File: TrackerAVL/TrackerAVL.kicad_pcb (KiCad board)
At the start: 2 copper layers, 174 parts, among them J801 Conn_02x07_Odd_Even, J802 Conn_01x15, J803 Conn_01x04, P201 uC_debug, Q201 DTC043ZEBTL, Q202 DTC043ZEBTL, Q203 DTC043ZEBTL, Q701 2N7002P, Q702 2N7002P, Q703 2N7002P, Q704 DTC043ZEBTL, U201 MAX3221, U202 LPC4337JBD144, U203 STS8C5H30L, U301 MPU-6050, U401 NAU8814, U501 STS8C5H30L, U502 LD1085D2T33R, U503 NCP114ASN180T1G, U601 MPCIE-Socket, U701 74LVC244APW, U801 74HC4053, X201 12MHz, X202 32.768K

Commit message: Cambios en pcb
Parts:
- moved D704 218.5 mm to (314.0, 128.9)
- moved D709 218.5 mm to (318.7, 126.6)
- moved Q701 218.5 mm to (309.2, 127.4)
- moved U301 218.5 mm to (301.2, 145.8)
- moved C302 218.5 mm to (304.2, 149.4)
- moved C304 218.5 mm to (300.4, 149.4)
- moved C501 218.5 mm to (252.3, 143.5)
- moved C502 218.5 mm to (262.6, 130.9)
- moved C503 218.5 mm to (252.3, 141.6)
- moved C506 218.5 mm to (262.6, 132.8)
- moved C701 218.5 mm to (321.9, 128.5)
- moved C702 218.5 mm to (309.9, 138.3)
- moved C703 218.5 mm to (314.7, 132.8)
- moved C704 218.5 mm to (309.9, 136.4)
- moved C705 218.5 mm to (317.4, 136.7)
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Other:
- board outline added: 100 x 70 mm
- net class Default: clearance 0.2 -> 0.25; via_dia 0.8 -> 1; via_drill 0.4 -> 0.5
- rule trace_clearance: 0.2 -> 0.25
- rule trace_min: 0.2 -> 0.25
- rule via_min_drill: 0.3 -> 0.4
- rule via_min_size: 0.4 -> 0.8
- board text added: "Equipo AVL vRaptor v1.0 Referencia: Mayer (Tecnología 8 mils) Grillas: 1mm, 0,5mm, 0,25mm Vía: 1mm - Agujero: 0,5mm Márgen: 0,25mm Pista más delgada: 0,25mm Dist. a borde: 0,3mm STACK-UP FR4 1,6mm Dual layer Componentes en capa superior Máscara anti-soldante: Azul Sin requerimientos especiales Terminación: HASL c/Pb Espesor de Cu: 1oz"

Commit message: Cambios en pcb
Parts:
- moved C404 239.4 mm to (112.3, 47.6)
- moved C405 239.4 mm to (108.6, 49.5)
- moved C410 239.4 mm to (116.1, 49.5)
- moved C418 239.4 mm to (112.3, 49.5)
- moved C419 239.4 mm to (116.1, 47.6)
- moved JP401 239.4 mm to (121.8, 55.7)
- moved R402 239.4 mm to (108.6, 47.6)
- moved R403 239.4 mm to (123.6, 47.6)
- moved R404 239.4 mm to (123.6, 49.5)
- moved R409 239.4 mm to (119.8, 49.5)
- moved R412 239.4 mm to (119.8, 47.6)
- moved U401 239.4 mm to (104.0, 49.3)
- moved C401 239.4 mm to (110.7, 51.5)
- moved C402 239.4 mm to (107.0, 54.9)
- moved C403 239.4 mm to (103.2, 56.8)
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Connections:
- J801 pad : (no net) -> GND
- Q201 pad 1: /CPU/SLEEP_MDM -> /CPU/LED1
- Q202 pad 1: /Acelerómetro/INT -> /CPU/LED2
- Q203 pad 1: /CPU/DISPLAY_MODE -> /CPU/LED3
- U202 pad 104: /CPU/SLEEP_MDM -> /CPU/LED1
- U202 pad 105: /Acelerómetro/INT -> /CPU/LED2
- U202 pad 106: /CPU/DISPLAY_MODE -> /CPU/LED3
- U202 pad 87: /Conectores_IO/PROG_TX -> /CPU/U3_TX
- U202 pad 88: /Conectores_IO/PROG_RX -> /CPU/U3_RX
- U202 pad 91: Net-(U202-Pad91) -> /CPU/SLEEP_MDM
- U202 pad 95: Net-(U202-Pad95) -> /Acelerómetro/INT
- U202 pad 96: Net-(U202-Pad96) -> /CPU/DISPLAY_MODE
- U601 pad 11: /Conectores_IO/PROG_TX -> /CPU/U3_TX
- U601 pad 13: /Conectores_IO/PROG_RX -> /CPU/U3_RX
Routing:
- net GND: track 0.00 -> 139.1 mm, vias 0 -> 4
- net +3V3: track 0.00 -> 45.7 mm, vias 0 -> 2
- net Net-(C502-Pad1): track 0.00 -> 40.3 mm, vias 0 -> 1
- net /VBAT: track 0.00 -> 25.0 mm
- net /Conectores_IO/PROG_TX: track 0.00 -> 23.1 mm, vias 0 -> 2
- net /Conectores_IO/PROG_RX: track 0.00 -> 22.2 mm, vias 0 -> 2
- net /IGN: track 0.00 -> 21.4 mm
- net Net-(C204-Pad2): track 0.00 -> 12.7 mm
- net Net-(C204-Pad1): track 0.00 -> 9.92 mm, vias 0 -> 2
- net +BATT: track 0.00 -> 7.74 mm
- net Net-(C205-Pad1): track 0.00 -> 7.53 mm, vias 0 -> 2
- net Net-(C205-Pad2): track 0.00 -> 7.06 mm
- net Net-(C210-Pad2): track 0.00 -> 5.91 mm
- net Net-(D501-Pad2): track 0.00 -> 5.38 mm
- net Net-(R501-Pad1): track 0.00 -> 2.95 mm
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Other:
- board size 100 x 70 mm -> 130 x 80 mm
- board text added: "Eje central"
- board text added: "Equipo AVL vRaptor v1.0 Referencia: Mayer (Tecnología 8 mils) Pistas: 1; 0,75; 0,5; 0,25 [mm] Vía: 1mm - Agujero: 0,5mm Márgen: 0,25mm Pista más delgada: 0,25mm Dist. a borde: 0,3mm STACK-UP FR4 1,6mm Dual layer Componentes en capa superior Máscara anti-soldante: Azul Sin requerimientos especiales Terminación: HASL c/Pb Espesor de Cu: 1oz"
- board text added: "Recomendaciones diseño > Cruces de pista entre capas a 90° > Colocar buenos planos de masa > Considerar poner vías térmicas > Uniones entre pads y pistas "teardrop" > Para plano de masa, clearance 0.25mm mínimo > Colocar jumpers-open para medir consumos"
- board text removed: "Equipo AVL vRaptor v1.0 Referencia: Mayer (Tecnología 8 mils) Grillas: 1mm, 0,5mm, 0,25mm Vía: 1mm - Agujero: 0,5mm Márgen: 0,25mm Pista más delgada: 0,25mm Dist. a borde: 0,3mm STACK-UP FR4 1,6mm Dual layer Componentes en capa superior Máscara anti-soldante: Azul Sin requerimientos especiales Terminación: HASL c/Pb Espesor de Cu: 1oz"

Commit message: Cambios en pcb
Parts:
- F103, F104, F105: moved to B.Cu
- moved R701 80.4 mm to (128.8, 129.7), turned to 270 degrees
- moved R702 78.8 mm to (131.0, 129.7), turned to 270 degrees
- moved Q701 77.7 mm to (131.5, 124.7), turned to 180 degrees
- moved R703 73.8 mm to (133.1, 129.7), turned to 270 degrees
- moved X201 73.6 mm to (191.6, 109.5)
- moved D701 72.0 mm to (127.2, 125.3), turned to 270 degrees
- moved D702 71.1 mm to (127.2, 120.4), turned to 90 degrees
- moved D703 70.8 mm to (127.2, 115.5), turned to 90 degrees
- moved Q702 66.1 mm to (131.5, 120.6), turned to 180 degrees
- moved D709 64.7 mm to (132.1, 109.1)
- moved FB202 64.7 mm to (202.1, 106.9), turned to 270 degrees
- moved R706 63.5 mm to (127.9, 111.1), turned to 180 degrees
- moved D707 63.5 mm to (163.5, 113.7)
- moved R707 62.5 mm to (127.9, 108.0), turned to 180 degrees
- moved C202 61.4 mm to (193.6, 112.4), turned to 270 degrees
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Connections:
- C701 pad 1: /DIG_IN_0 -> /CPU/DIG_IN_0
- C702 pad 1: /DIG_IN_1 -> /CPU/DIG_IN_1
- C703 pad 1: /DIG_IN_2 -> /CPU/DIG_IN_2
- D704 pad 1: /DIG_IN_0 -> /CPU/DIG_IN_0
- D705 pad 1: /DIG_IN_1 -> /CPU/DIG_IN_1
- D706 pad 1: /DIG_IN_2 -> /CPU/DIG_IN_2
- J801 pad : GND -> (no net)
- U202 pad 85: /DIG_IN_0 -> /CPU/DIG_IN_0
- U202 pad 86: /DIG_IN_1 -> /CPU/DIG_IN_1
- U202 pad 97: /DIG_IN_2 -> /CPU/DIG_IN_2
- U701 pad 14: /DIG_IN_2 -> /CPU/DIG_IN_2
- U701 pad 16: /DIG_IN_1 -> /CPU/DIG_IN_1
- U701 pad 18: /DIG_IN_0 -> /CPU/DIG_IN_0
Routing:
- net GND: track 139.1 -> 272.6 mm
- net +3V3: track 45.7 -> 87.5 mm, vias 2 -> 49
- net /DIG_IN_0: track 0.00 -> 35.6 mm, vias 0 -> 2
- net /DIG_IN_1: track 0.00 -> 33.5 mm, vias 0 -> 2
- net /DIG_IN_2: track 0.00 -> 30.1 mm, vias 0 -> 2
- net /MIC+: track 0.00 -> 19.6 mm
- net /CPU/BUZZER: track 0.00 -> 17.3 mm
- net /Conectores_IO/DISP_2: track 0.00 -> 16.3 mm
- net /Conectores_IO/DISP_1: track 0.00 -> 15.3 mm
- net /Conectores_IO/DISP_0: track 0.00 -> 14.9 mm
- net /CPU/IBUTTON: track 0.00 -> 13.8 mm
- net /CPU/DIG_OUT_2: track 0.00 -> 13.5 mm
- net /MIC-: track 0.00 -> 11.4 mm
- net Net-(FB202-Pad1): track 0.00 -> 10.5 mm
- net /CPU/XTAL1: track 0.00 -> 10.2 mm
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- added copper zone on B.Cu, net +3V3
- added copper zone on F.Cu, net +3V3
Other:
- rule trace_min: 0.25 -> 0.2
- board text added: "Recomendaciones diseño > Cruces de pista entre capas a 90° > Colocar buenos planos de masa > Considerar poner vías térmicas > Uniones entre pads y pistas "teardrop" > Para plano de masa, clearance 0.25mm mínimo > Colocar jumpers-open para medir consumos > Orientación silkscreen "para un mismo lado""
- board text removed: "Recomendaciones diseño > Cruces de pista entre capas a 90° > Colocar buenos planos de masa > Considerar poner vías térmicas > Uniones entre pads y pistas "teardrop" > Para plano de masa, clearance 0.25mm mínimo > Colocar jumpers-open para medir consumos"

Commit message: Cambios en pcb
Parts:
- moved C302 95.2 mm to (173.5, 75.4), turned to 180 degrees
- moved C303 90.9 mm to (173.5, 77.5), turned to 180 degrees
- moved U301 87.9 mm to (178.8, 76.1), turned to 270 degrees
- moved JP203 85.8 mm to (221.1, 135.1)
- moved C304 85.7 mm to (179.7, 81.4), turned to 270 degrees
- moved C301 83.9 mm to (177.5, 81.4), turned to 270 degrees
- moved JP202 79.1 mm to (221.1, 119.7)
- moved C229 67.9 mm to (215.4, 95.0)
- moved C228 67.2 mm to (215.4, 101.5)
- moved C227 63.5 mm to (215.4, 103.7)
- moved R205 59.3 mm to (206.4, 106.9), turned to 270 degrees
- moved R218 56.6 mm to (211.4, 95.0)
- moved R210 55.5 mm to (215.4, 99.3), turned to 180 degrees
- moved R212 54.6 mm to (211.4, 99.3)
- moved R208 54.5 mm to (211.4, 101.5)
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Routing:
- net +3V3: track 87.5 -> 196.1 mm, vias 49 -> 50
- net GND: track 272.6 -> 378.7 mm, vias 4 -> 28
- net /CPU/PWR_MDM: track 0.00 -> 27.7 mm
- net /I2C_SCL: track 0.00 -> 23.2 mm, vias 0 -> 2
- net /CPU/TDI: track 0.00 -> 20.3 mm
- net /I2C_SDA: track 0.00 -> 18.5 mm
- net /CPU/TCK: track 0.00 -> 18.4 mm, vias 0 -> 2
- net /CPU/TDO: track 0.00 -> 16.1 mm
- net /CPU/PERST: track 0.00 -> 12.9 mm
- net /CPU/TMS: track 0.00 -> 11.5 mm
- net Net-(R205-Pad1): track 0.00 -> 7.31 mm
- net /CPU/DIG_IN_0: track 2.17 -> 8.99 mm
- net Net-(R204-Pad1): track 0.00 -> 5.46 mm
- net /CPU/TEC_3: track 0.00 -> 4.10 mm
- net /CPU/TEC_2: track 0.00 -> 4.10 mm
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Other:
- board text added: "Equipo AVL vRaptor v1.0 Referencia: Mayer (Tecnología 8 mils) Pistas: 1,5; 1; 0,75; 0,5; 0,25 [mm] Vía: 1mm - Agujero: 0,5mm Márgen: 0,25mm Pista más delgada: 0,25mm Dist. a borde: 0,3mm STACK-UP FR4 1,6mm Dual layer Componentes en capa superior Máscara anti-soldante: Azul Sin requerimientos especiales Terminación: HASL c/Pb Espesor de Cu: 1oz"
- board text removed: "Equipo AVL vRaptor v1.0 Referencia: Mayer (Tecnología 8 mils) Pistas: 1; 0,75; 0,5; 0,25 [mm] Vía: 1mm - Agujero: 0,5mm Márgen: 0,25mm Pista más delgada: 0,25mm Dist. a borde: 0,3mm STACK-UP FR4 1,6mm Dual layer Componentes en capa superior Máscara anti-soldante: Azul Sin requerimientos especiales Terminación: HASL c/Pb Espesor de Cu: 1oz"

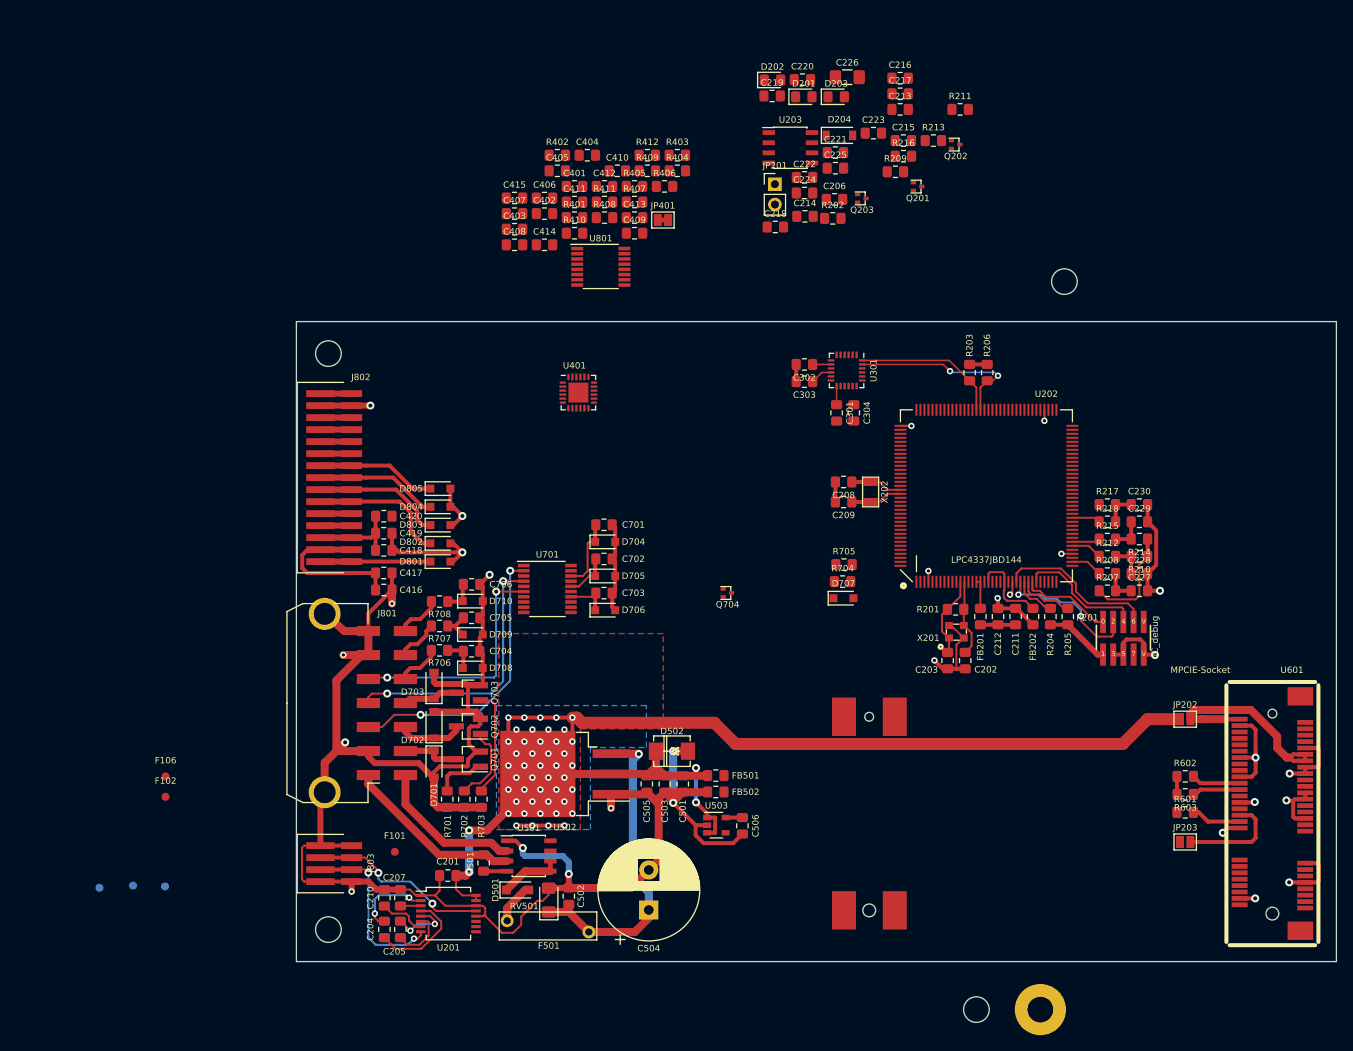
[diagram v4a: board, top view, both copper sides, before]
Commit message: Cambios en pcb y modelos 3d
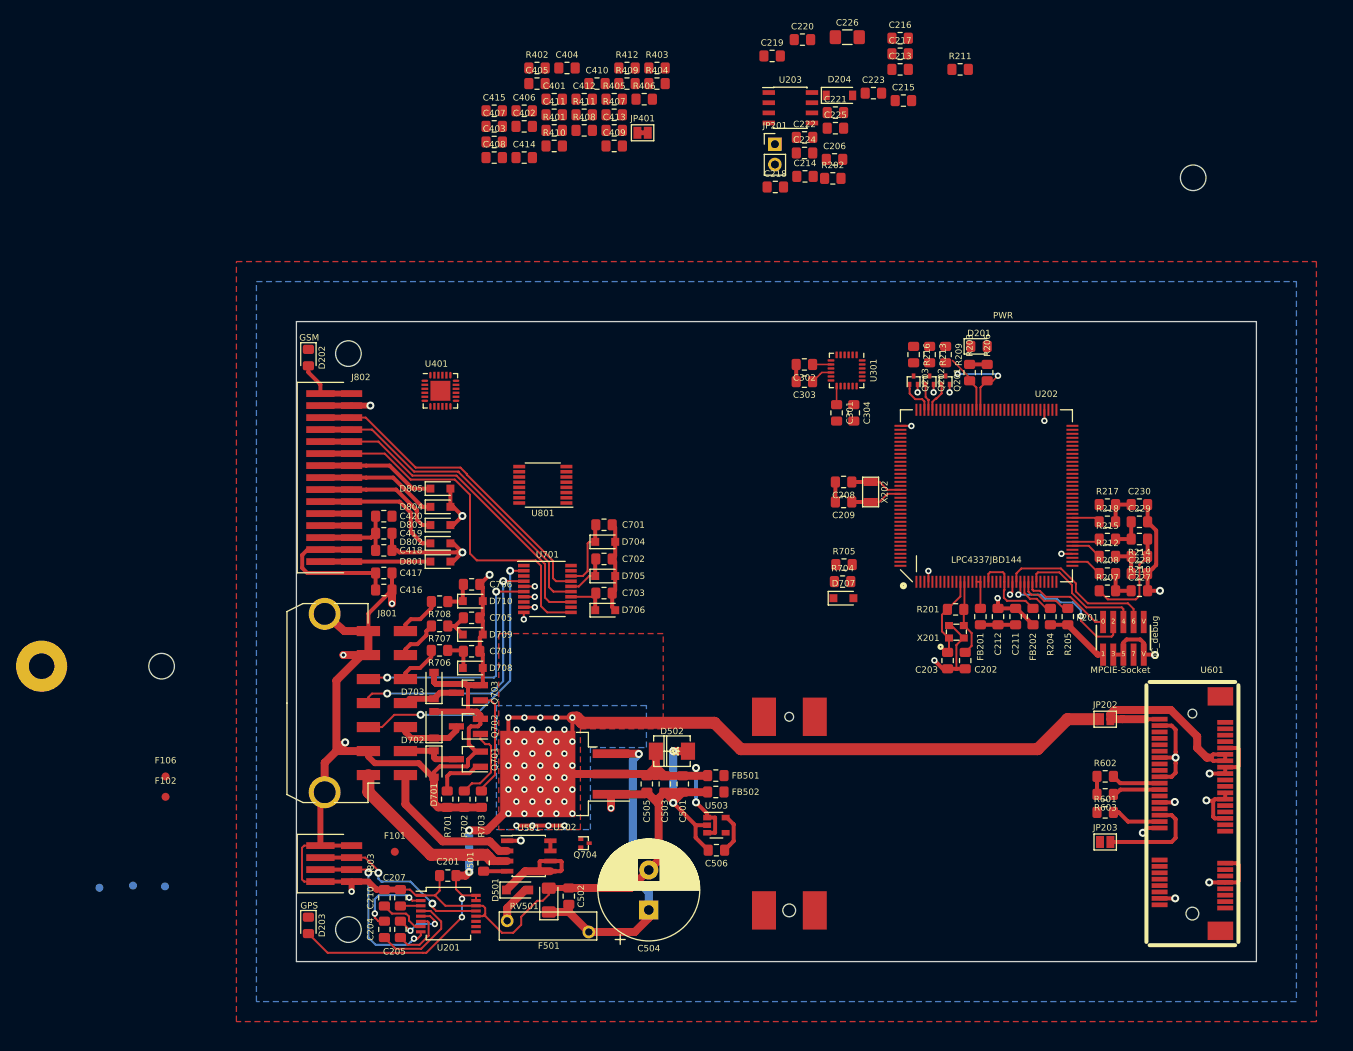
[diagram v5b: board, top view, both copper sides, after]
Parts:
- moved TP101 132.0 mm to (78.2, 113.1)
- moved D203 122.8 mm to (111.5, 145.5), turned to 270 degrees
- moved H102 110.5 mm to (93.2, 113.1)
- moved D202 67.6 mm to (111.5, 74.5), turned to 270 degrees
- moved D201 38.1 mm to (195.3, 73.1)
- moved Q704 36.0 mm to (145.6, 135.7)
- moved Q202 29.6 mm to (189.7, 77.8), turned to 90 degrees
- moved U801 28.2 mm to (140.8, 90.4), turned to 180 degrees
- moved R213 26.8 mm to (189.2, 74.1), turned to 270 degrees
- moved R216 24.8 mm to (187.2, 74.1), turned to 270 degrees
- moved Q201 24.6 mm to (191.7, 77.8), turned to 90 degrees
- moved Q203 24.0 mm to (187.7, 77.8), turned to 90 degrees
- moved R209 23.7 mm to (191.2, 74.1), turned to 270 degrees
- moved H103 20.7 mm to (222.1, 52.0)
- moved U401 17.3 mm to (128.0, 78.7)
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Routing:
- net /TEC_3: track 3.90 -> 46.8 mm
- net /TEC_2: track 3.90 -> 42.1 mm
- net /TEC_1: track 3.90 -> 41.5 mm
- net /TEC_0: track 3.90 -> 41.1 mm
- net +3V3: track 196.1 -> 215.5 mm, vias 50 -> 52
- net /I2C_SCL: track 23.2 -> 10.7 mm
- net GND: track 378.7 -> 367.6 mm, vias 28 -> 31
- net /I2C_SDA: track 18.5 -> 7.41 mm
- net /VBAT: track 22.5 -> 32.4 mm
- net +BATT: track 7.74 -> 13.0 mm
- net /CPU/LED3: track 0.00 -> 4.45 mm
- net /CPU/LED1: track 0.00 -> 3.71 mm
- net /CPU/LED2: track 0.00 -> 3.33 mm
- net +1V8: track 4.34 -> 7.30 mm
- net /CPU/TEC_3: track 4.10 -> 5.48 mm, vias 0 -> 1
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- added copper zone on B.Cu, net GND
- added copper zone on F.Cu, net GND
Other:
- board size 130 x 80 mm -> 120 x 80 mm
- board text added: "GPS"
- board text added: "GSM"
- board text added: "PWR"

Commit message: Cambios en pcb
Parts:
- moved D707 5.90 mm to (181.6, 99.6)
- moved U801 3.55 mm to (139.7, 93.8)
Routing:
- net /Conectores_IO/DISP_2: track 16.3 -> 33.7 mm, vias 0 -> 2
- net /Conectores_IO/DISP_0: track 14.9 -> 27.2 mm, vias 0 -> 2
- net /Conectores_IO/DISP_1: track 15.3 -> 26.2 mm, vias 0 -> 2
- net /TEC_2: track 42.1 -> 46.4 mm
- net /TEC_1: track 41.5 -> 45.8 mm
- net /TEC_0: track 41.1 -> 45.3 mm
- net /CPU/DISPLAY_MODE: track 0.00 -> 1.30 mm
- net GND: track 367.6 -> 366.3 mm, vias 31 -> 29
